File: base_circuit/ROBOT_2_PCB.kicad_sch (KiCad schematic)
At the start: 44 parts, among them J1 Conn_01x04, J2 Conn_01x02_Male, J3 Conn_01x01_Female, J4 M1,2, J5 M3,4, J6 Conn_01x02_Male, J7 Conn_01x02_Male, M1 Conn_01x04_Female, M2 Conn_01x04_Female, M3 Conn_01x04_Female, M4 Conn_01x04_Female, SW1 SW_SPDT, SW2 SW_SPDT

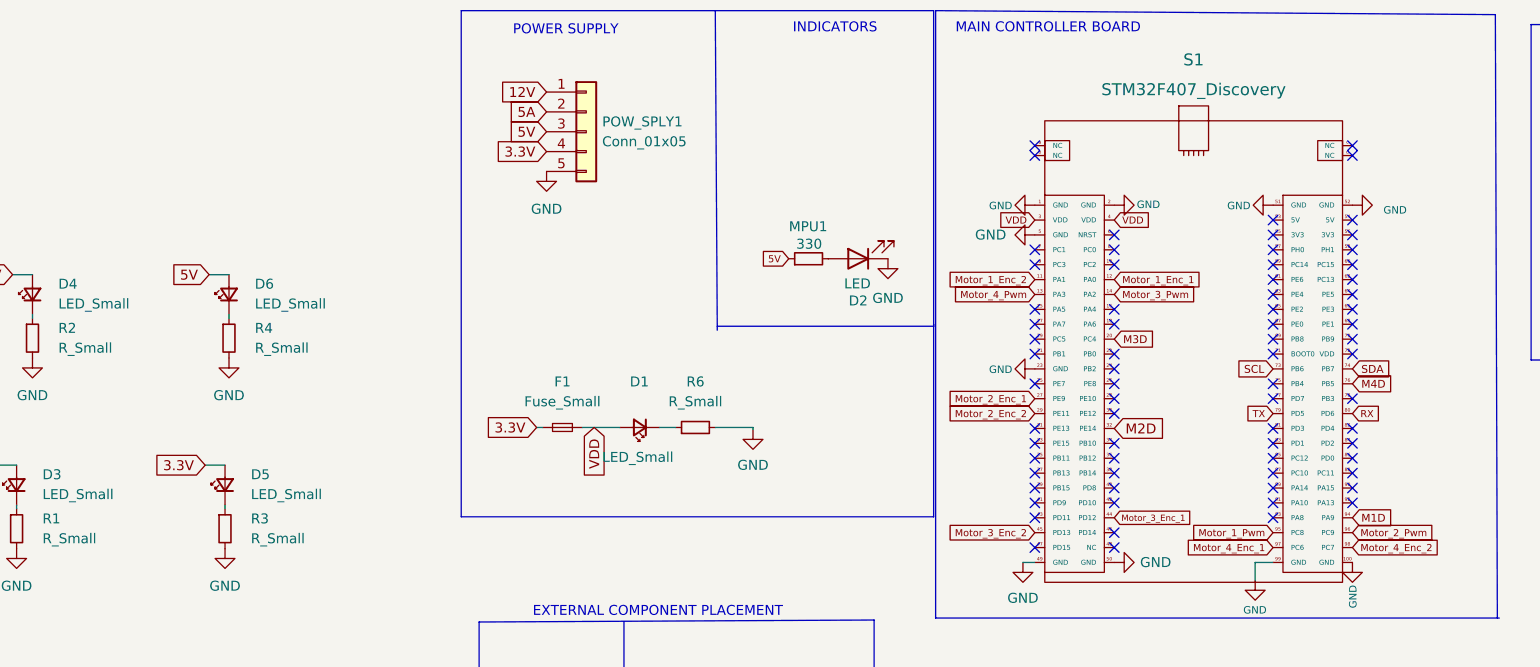
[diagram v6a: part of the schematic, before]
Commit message: Redesign Base Circuit complete
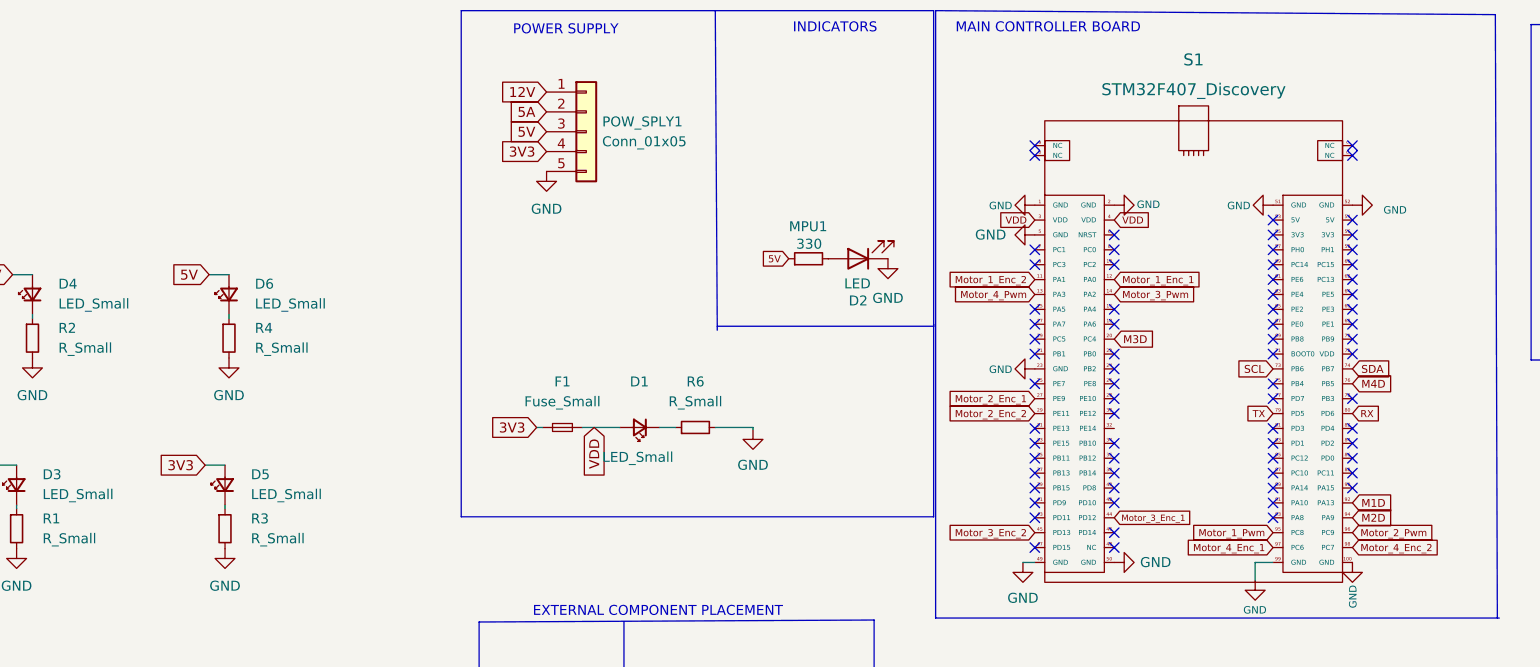
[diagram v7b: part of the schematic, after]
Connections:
- net 3.3V is gone; now on net 3V3: D5.2 (A), F1.1, POW_SPLY1.4 (Pin_4)
- net M1D: now also S1.92 (PA13); no longer S1.94 (PA9)
- net M2D: now also S1.94 (PA9); no longer S1.32 (PE14)
- no-connect marks 72 -> 71
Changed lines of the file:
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@@
   (no_connect (at 119.888 72.898))
   (no_connect (at 89.408 72.898))
-  (no_connect (at 130.048 80.518))
   (no_connect (at 130.048 55.753))
   (no_connect (at 130.048 72.898))
@@
     )
   )
-  (global_label "M2D" (shape input) (at 99.568 70.993 0) (fields_autoplaced)
-    (effects (font (size 1.27 1.27)) (justify left))
-    (property "Intersheet References" "${INTERSHEET_REFS}" (id 0) (at 105.9121 70.9136 0)
-      (effects (font (size 1.27 1.27)) (justify left) hide)
-    )
-  )
   (global_label "Motor_2_Enc_2" (shape input) (at 128.778 120.904 180) (fields_autoplaced)
     (effects (font (size 0.9 0.9)) (justify right))
@@
     (property "Intersheet References" "${INTERSHEET_REFS}" (id 0) (at 109.178 84.2718 0)
       (effects (font (size 0.9 0.9)) (justify right) hide)
+    )
+  )
+  (global_label "M1D" (shape input) (at 130.048 80.518 0) (fields_autoplaced)
+    (effects (font (size 1 1)) (justify left))
+    (property "Intersheet References" "${INTERSHEET_REFS}" (id 0) (at 135.0432 80.4555 0)
+      (effects (font (size 1 1)) (justify left) hide)
     )
   )
@@
     )
   )
-  (global_label "3.3V" (shape input) (at -16.764 75.692 180) (fields_autoplaced)
-    (effects (font (size 1.27 1.27)) (justify right))
-    (property "Intersheet References" "${INTERSHEET_REFS}" (id 0) (at -23.2895 75.6126 0)
+  (global_label "3V3" (shape input) (at -16.764 75.692 180) (fields_autoplaced)
+    (effects (font (size 1.27 1.27)) (justify right))
+    (property "Intersheet References" "${INTERSHEET_REFS}" (id 0) (at -22.6847 75.6126 0)
       (effects (font (size 1.27 1.27)) (justify right) hide)
     )
@@
     )
   )
-  (global_label "3.3V" (shape input) (at 25.654 70.866 180) (fields_autoplaced)
-    (effects (font (size 1.27 1.27)) (justify right))
-    (property "Intersheet References" "${INTERSHEET_REFS}" (id 0) (at 19.1285 70.9454 0)
+  (global_label "3V3" (shape input) (at 25.654 70.866 180) (fields_autoplaced)
+    (effects (font (size 1.27 1.27)) (justify right))
+    (property "Intersheet References" "${INTERSHEET_REFS}" (id 0) (at 19.7333 70.7866 0)
       (effects (font (size 1.27 1.27)) (justify right) hide)
     )
@@
     )
   )
-  (global_label "3.3V" (shape input) (at 26.924 35.56 180) (fields_autoplaced)
-    (effects (font (size 1.27 1.27)) (justify right))
-    (property "Intersheet References" "${INTERSHEET_REFS}" (id 0) (at 20.3985 35.6394 0)
+  (global_label "3V3" (shape input) (at 26.924 35.56 180) (fields_autoplaced)
+    (effects (font (size 1.27 1.27)) (justify right))
+    (property "Intersheet References" "${INTERSHEET_REFS}" (id 0) (at 21.0033 35.4806 0)
       (effects (font (size 1.27 1.27)) (justify right) hide)
     )
@@
     )
   )
-  (global_label "M1D" (shape input) (at 130.048 82.423 0) (fields_autoplaced)
+  (global_label "M2D" (shape input) (at 130.048 82.423 0) (fields_autoplaced)
     (effects (font (size 1 1)) (justify left))
     (property "Intersheet References" "${INTERSHEET_REFS}" (id 0) (at 135.0432 82.3605 0)
